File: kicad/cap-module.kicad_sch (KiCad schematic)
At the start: 4 parts, among them U1 RaspberryPi_Pico, U2 AD7747

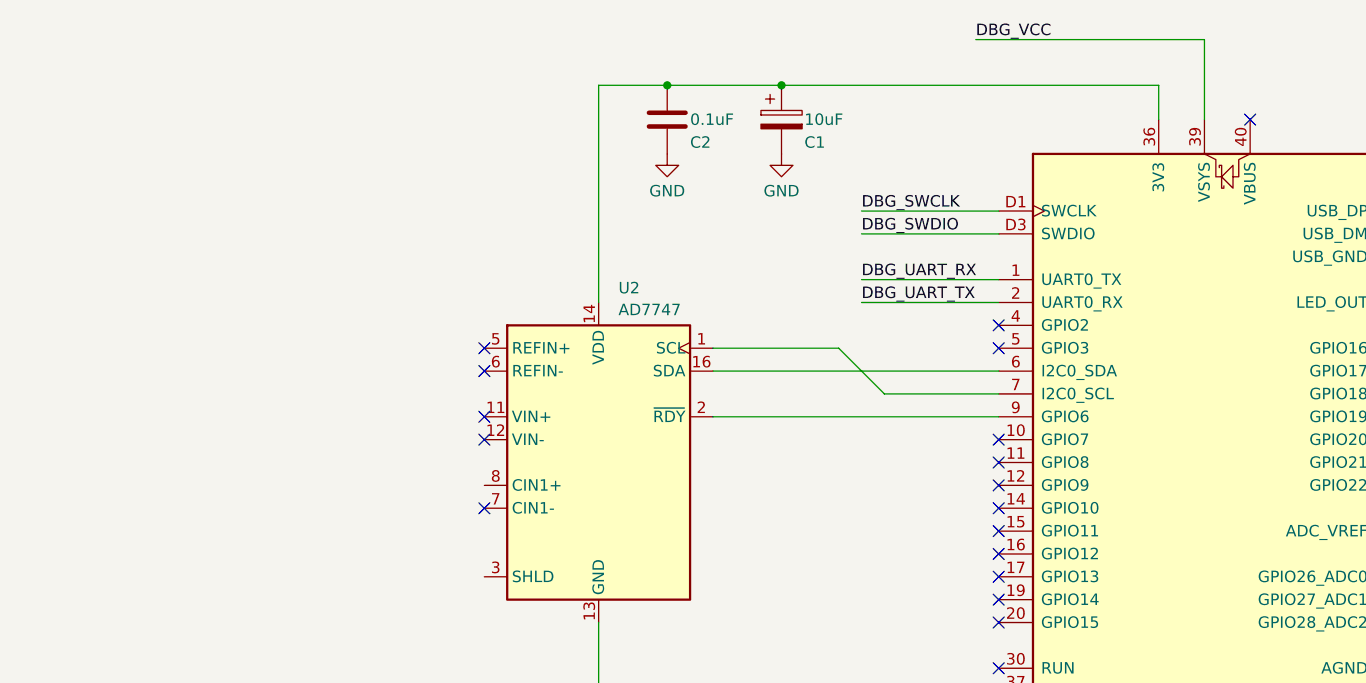
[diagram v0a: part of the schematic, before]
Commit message: Add capacitor socket
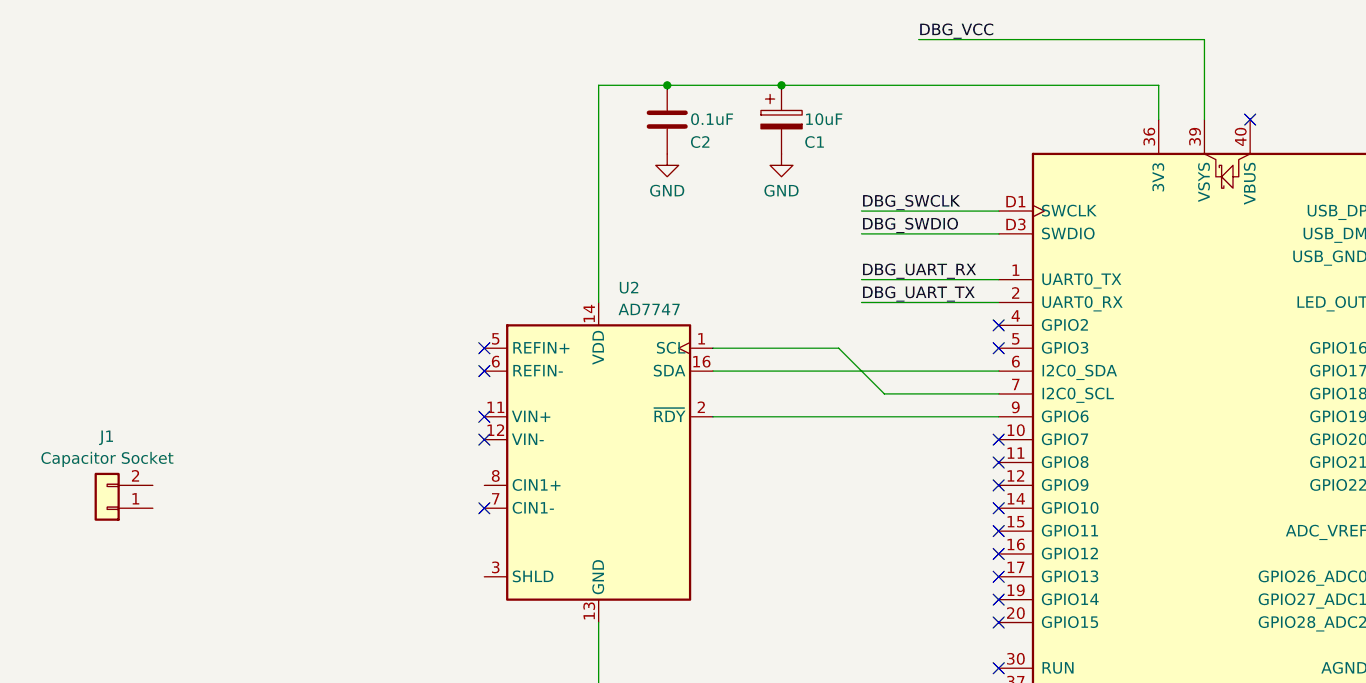
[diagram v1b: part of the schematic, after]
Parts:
- added J1: Capacitor Socket, symbol Connector_Generic:Conn_01x02
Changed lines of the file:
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@@
     (stroke (width 0) (type default))
   )
-  (wire (pts (xy 133.35 50.8) (xy 158.75 50.8))
+  (wire (pts (xy 127 50.8) (xy 158.75 50.8))
     (stroke (width 0) (type default))
   )
@@
     (effects (font (size 1.27 1.27)) (justify left bottom))
   )
-  (label "DBG_VCC" (at 133.35 50.8 0) (fields_autoplaced)
+  (label "DBG_VCC" (at 127 50.8 0) (fields_autoplaced)
     (effects (font (size 1.27 1.27)) (justify left bottom))
   )
@@
         )
       )
+    )
+  )
+  (symbol (lib_id "Connector_Generic:Conn_01x02") (at 36.83 102.87 180) (unit 1)
+    (in_bom yes) (on_board yes) (dnp no) (fields_autoplaced)
+    (property "Reference" "J1" (at 36.83 94.9157 0)
+      (effects (font (size 1.27 1.27)))
+    )
+    (property "Value" "Capacitor Socket" (at 36.83 97.3399 0)
+      (effects (font (size 1.27 1.27)))
+    )
+    (property "Footprint" "" (at 36.83 102.87 0)
+      (effects (font (size 1.27 1.27)) hide)
+    )
+    (property "Datasheet" "~" (at 36.83 102.87 0)
+      (effects (font (size 1.27 1.27)) hide)
+    )
+    (pin "1")
+    (pin "2")
+    (instances
+      (project "cap-module"
+        (path "/2da8fa58-ccef-42b1-8320-baeb3fec91e3"
+          (reference "J1") (unit 1)
+        )
+      )

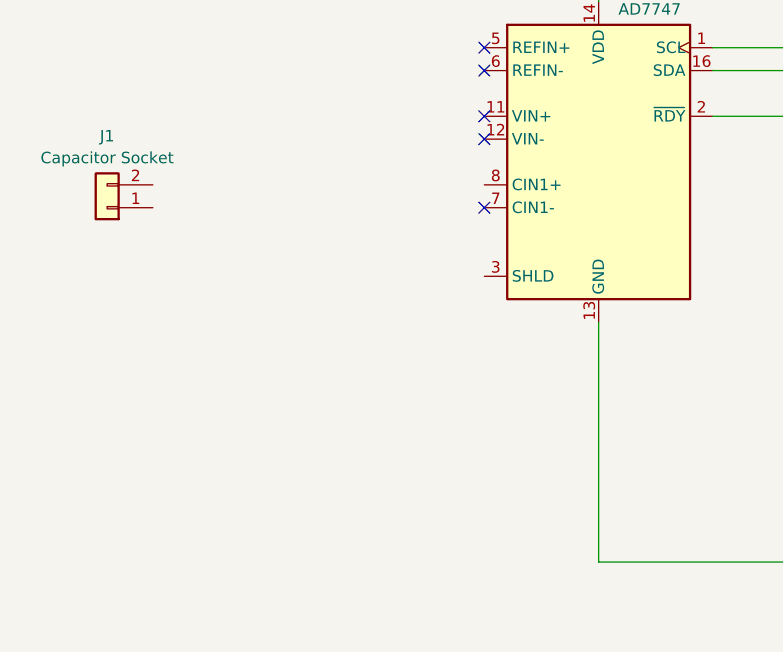
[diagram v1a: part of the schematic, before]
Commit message: Add shielded net & connect capacitor socket
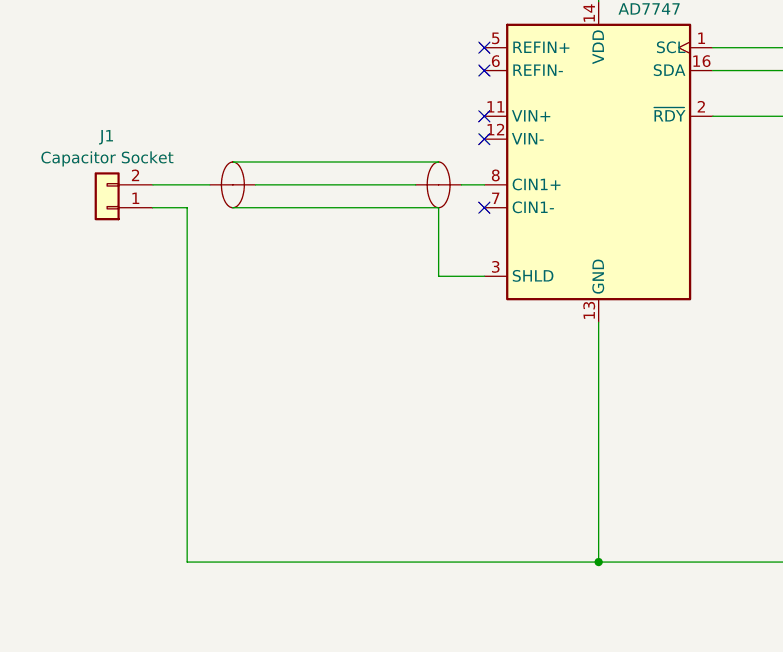
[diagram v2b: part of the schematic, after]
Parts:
- added NS1, NS2: NetShield_1-2SH, symbol Device_NetShield:NetShield_1-2SH
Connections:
- net GND: now also J1.1 (Pin_1)
- net at U2.3 (SHLD): now also NS1.2 (Shield), NS2.2 (Shield)
- net at U2.8 (CIN1+): now also NS1.1
- net at J1.2 (Pin_2): now also NS2.1
- new net: NS1.1, NS2.1
- new net: NS1.2 (Shield), NS2.2 (Shield)
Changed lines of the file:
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@@
   (junction (at 111.76 55.88) (diameter 0) (color 0 0 0 0)
+  )
+  (junction (at 91.44 142.24) (diameter 0) (color 0 0 0 0)
   )
   (junction (at 99.06 55.88) (diameter 0) (color 0 0 0 0)
@@
     (stroke (width 0) (type default))
   )
+  (wire (pts (xy 78.74 100.33) (xy 76.2 100.33))
+    (stroke (width 0) (type default))
+  )
   (wire (pts (xy 91.44 55.88) (xy 99.06 55.88))
     (stroke (width 0) (type default))
   )
+  (wire (pts (xy 45.72 102.87) (xy 45.72 142.24))
+    (stroke (width 0) (type default))
+  )
+  (wire (pts (xy 158.75 50.8) (xy 158.75 59.69))
+    (stroke (width 0) (type default))
+  )
+  (wire (pts (xy 73.66 110.49) (xy 78.74 110.49))
+    (stroke (width 0) (type default))
+  )
+  (wire (pts (xy 153.67 55.88) (xy 153.67 59.69))
+    (stroke (width 0) (type default))
+  )
+  (wire (pts (xy 104.14 85.09) (xy 118.11 85.09))
+    (stroke (width 0) (type default))
+  )
+  (wire (pts (xy 45.72 142.24) (xy 91.44 142.24))
+    (stroke (width 0) (type default))
+  )
+  (wire (pts (xy 41.91 102.87) (xy 45.72 102.87))
+    (stroke (width 0) (type default))
+  )
+  (wire (pts (xy 118.11 85.09) (xy 123.19 90.17))
+    (stroke (width 0) (type default))
+  )
+  (wire (pts (xy 111.76 55.88) (xy 153.67 55.88))
+    (stroke (width 0) (type default))
+  )
+  (wire (pts (xy 127 144.78) (xy 127 142.24))
+    (stroke (width 0) (type default))
+  )
+  (wire (pts (xy 53.34 100.33) (xy 71.12 100.33))
+    (stroke (width 0) (type default))
+  )
+  (wire (pts (xy 158.75 138.43) (xy 158.75 142.24))
+    (stroke (width 0) (type default))
+  )
+  (wire (pts (xy 99.06 55.88) (xy 111.76 55.88))
+    (stroke (width 0) (type default))
+  )
+  (wire (pts (xy 50.8 102.87) (xy 73.66 102.87))
+    (stroke (width 0) (type dash))
+  )
+  (wire (pts (xy 91.44 55.88) (xy 91.44 80.01))
+    (stroke (width 0) (type default))
+  )
+  (wire (pts (xy 120.65 72.39) (xy 135.89 72.39))
+    (stroke (width 0) (type default))
+  )
+  (wire (pts (xy 123.19 90.17) (xy 135.89 90.17))
+    (stroke (width 0) (type default))
+  )
+  (wire (pts (xy 48.26 100.33) (xy 41.91 100.33))
+    (stroke (width 0) (type default))
+  )
+  (wire (pts (xy 120.65 77.47) (xy 135.89 77.47))
+    (stroke (width 0) (type default))
+  )
+  (wire (pts (xy 120.65 80.01) (xy 135.89 80.01))
+    (stroke (width 0) (type default))
+  )
+  (wire (pts (xy 127 142.24) (xy 158.75 142.24))
+    (stroke (width 0) (type default))
+  )
+  (wire (pts (xy 91.44 142.24) (xy 127 142.24))
+    (stroke (width 0) (type default))
+  )
+  (wire (pts (xy 127 50.8) (xy 158.75 50.8))
+    (stroke (width 0) (type default))
+  )
+  (wire (pts (xy 73.66 110.49) (xy 73.66 102.87))
+    (stroke (width 0) (type default))
+  )
+  (wire (pts (xy 50.8 97.79) (xy 73.66 97.79))
+    (stroke (width 0) (type dash))
+  )
   (wire (pts (xy 91.44 115.57) (xy 91.44 142.24))
     (stroke (width 0) (type default))
   )
-  (wire (pts (xy 158.75 50.8) (xy 158.75 59.69))
-    (stroke (width 0) (type default))
-  )
-  (wire (pts (xy 153.67 55.88) (xy 153.67 59.69))
-    (stroke (width 0) (type default))
-  )
-  (wire (pts (xy 104.14 85.09) (xy 118.11 85.09))
-    (stroke (width 0) (type default))
-  )
-  (wire (pts (xy 118.11 85.09) (xy 123.19 90.17))
-    (stroke (width 0) (type default))
-  )
-  (wire (pts (xy 111.76 55.88) (xy 153.67 55.88))
-    (stroke (width 0) (type default))
-  )
-  (wire (pts (xy 127 144.78) (xy 127 142.24))
-    (stroke (width 0) (type default))
-  )
-  (wire (pts (xy 158.75 138.43) (xy 158.75 142.24))
-    (stroke (width 0) (type default))
-  )
-  (wire (pts (xy 99.06 55.88) (xy 111.76 55.88))
-    (stroke (width 0) (type default))
-  )
-  (wire (pts (xy 91.44 55.88) (xy 91.44 80.01))
-    (stroke (width 0) (type default))
-  )
-  (wire (pts (xy 120.65 72.39) (xy 135.89 72.39))
-    (stroke (width 0) (type default))
-  )
-  (wire (pts (xy 123.19 90.17) (xy 135.89 90.17))
-    (stroke (width 0) (type default))
-  )
-  (wire (pts (xy 120.65 77.47) (xy 135.89 77.47))
-    (stroke (width 0) (type default))
-  )
-  (wire (pts (xy 120.65 80.01) (xy 135.89 80.01))
-    (stroke (width 0) (type default))
-  )
-  (wire (pts (xy 127 142.24) (xy 158.75 142.24))
-    (stroke (width 0) (type default))
-  )
-  (wire (pts (xy 91.44 142.24) (xy 127 142.24))
-    (stroke (width 0) (type default))
-  )
-  (wire (pts (xy 127 50.8) (xy 158.75 50.8))
-    (stroke (width 0) (type default))
-  )
   (wire (pts (xy 120.65 69.85) (xy 135.89 69.85))
     (stroke (width 0) (type default))
@@
   (label "DBG_SWDIO" (at 120.65 72.39 0) (fields_autoplaced)
     (effects (font (size 1.27 1.27)) (justify left bottom))
+  )
+  (symbol (lib_id "Device_NetShield:NetShield_1-2SH") (at 73.66 100.33 0) (unit 1)
+    (in_bom no) (on_board yes) (dnp no) (fields_autoplaced)
+    (property "Reference" "NS1" (at 72.39 96.52 0)
+      (effects (font (size 1.27 1.27)) (justify right) hide)
+    )
+    (property "Value" "NetShield_1-2SH" (at 72.39 104.14 0)
+      (effects (font (size 1.27 1.27)) (justify right) hide)
+    )
+    (property "Footprint" "" (at 73.66 100.33 0)
+      (effects (font (size 1.27 1.27)) hide)
+    )
+    (property "Datasheet" "~" (at 73.66 109.22 0)
+      (effects (font (size 1.27 1.27)) hide)
+    )
+    (pin "1")
+    (pin "1")
+    (pin "2")
+    (pin "2")
+    (instances
+      (project "cap-module"
+        (path "/2da8fa58-ccef-42b1-8320-baeb3fec91e3"
+          (reference "NS1") (unit 1)
+        )
+      )
+    )
   )
   (symbol (lib_id "Device:C") (at 99.06 59.69 0) (unit 1)
@@
         )
       )
+    )
+  )
+  (symbol (lib_id "Device_NetShield:NetShield_1-2SH") (at 50.8 100.33 0) (unit 1)
+    (in_bom no) (on_board yes) (dnp no) (fields_autoplaced)
+    (property "Reference" "NS2" (at 49.53 96.52 0)
+      (effects (font (size 1.27 1.27)) (justify right) hide)
+    )
+    (property "Value" "NetShield_1-2SH" (at 49.53 104.14 0)
+      (effects (font (size 1.27 1.27)) (justify right) hide)
+    )
+    (property "Footprint" "" (at 50.8 100.33 0)
+      (effects (font (size 1.27 1.27)) hide)
+    )
+    (property "Datasheet" "~" (at 50.8 109.22 0)
+      (effects (font (size 1.27 1.27)) hide)
+    )
+    (pin "1")
+    (pin "1")
+    (pin "2")
+    (pin "2")
+    (instances
+      (project "cap-module"
+        (path "/2da8fa58-ccef-42b1-8320-baeb3fec91e3"
+          (reference "NS2") (unit 1)
+        )
+      )

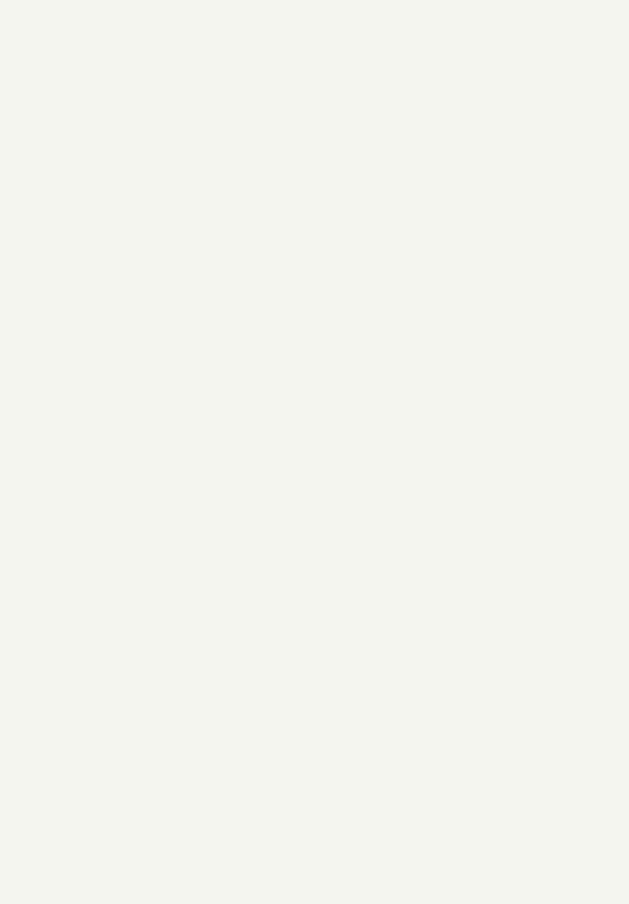
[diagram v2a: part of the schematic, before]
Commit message: Add Picoprobe
Set alternate pin assignments

Note that GND was set to an Input to play nice with the
already-outputting Pico, even though in some cases the Picoprobe
will be supplying power and ground to the system.
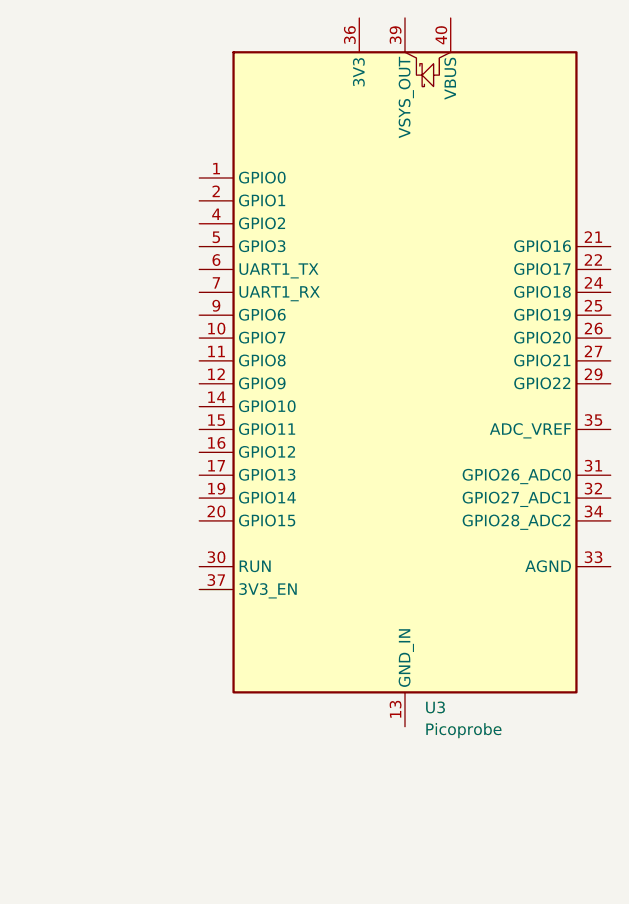
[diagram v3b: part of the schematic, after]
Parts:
- added U3: Picoprobe, Module_RaspberryPi_Pico:RaspberryPi_Pico_Common, symbol MCU_Module_RaspberryPi_Pico:RaspberryPi_Pico
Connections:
- net at NS1.2 (Shield), NS2.2 (Shield): no longer U2.3 (SHLD)
- new net: NS1.2 (Shield), NS2.2 (Shield), U2.3 (SHLD)
- new net: U3.13 (GND), U3.18 (GND), U3.23 (GND), U3.28 (GND), U3.3 (GND), U3.38 (GND), U3.8 (GND)
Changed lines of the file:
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@@
+    )
+  )
+  (symbol (lib_id "MCU_Module_RaspberryPi_Pico:RaspberryPi_Pico") (at 247.65 74.93 0) (unit 1)
+    (in_bom yes) (on_board no) (dnp no) (fields_autoplaced)
+    (property "Reference" "U3" (at 249.8441 110.9401 0)
+      (effects (font (size 1.27 1.27)) (justify left))
+    )
+    (property "Value" "Picoprobe" (at 249.8441 113.3643 0)
+      (effects (font (size 1.27 1.27)) (justify left))
+    )
+    (property "Footprint" "Module_RaspberryPi_Pico:RaspberryPi_Pico_Common" (at 247.65 124.46 0)
+      (effects (font (size 1.27 1.27)) hide)
+    )
+    (property "Datasheet" "https://datasheets.raspberrypi.com/pico/pico-datasheet.pdf" (at 247.65 127 0)
+      (effects (font (size 1.27 1.27)) hide)
+    )
+    (pin "1")
+    (pin "10")
+    (pin "11")
+    (pin "12")
+    (pin "13" (alternate "GND_IN"))
+    (pin "14")
+    (pin "15")
+    (pin "16")
+    (pin "17")
+    (pin "18")
+    (pin "19")
+    (pin "2")
+    (pin "20")
+    (pin "21")
+    (pin "22")
+    (pin "23")
+    (pin "24")
+    (pin "25")
+    (pin "26")
+    (pin "27")
+    (pin "28")
+    (pin "29")
+    (pin "3")
+    (pin "30")
+    (pin "31")
+    (pin "32")
+    (pin "33")
+    (pin "34")
+    (pin "35")
+    (pin "36")
+    (pin "37")
+    (pin "38")
+    (pin "39" (alternate "VSYS_OUT"))
+    (pin "4")
+    (pin "40")
+    (pin "5")
+    (pin "6" (alternate "UART1_TX"))
+    (pin "7" (alternate "UART1_RX"))
+    (pin "8")
+    (pin "9")
+    (instances
+      (project "cap-module"
+        (path "/2da8fa58-ccef-42b1-8320-baeb3fec91e3"
+          (reference "U3") (unit 1)
+        )
+      )
     )
   )

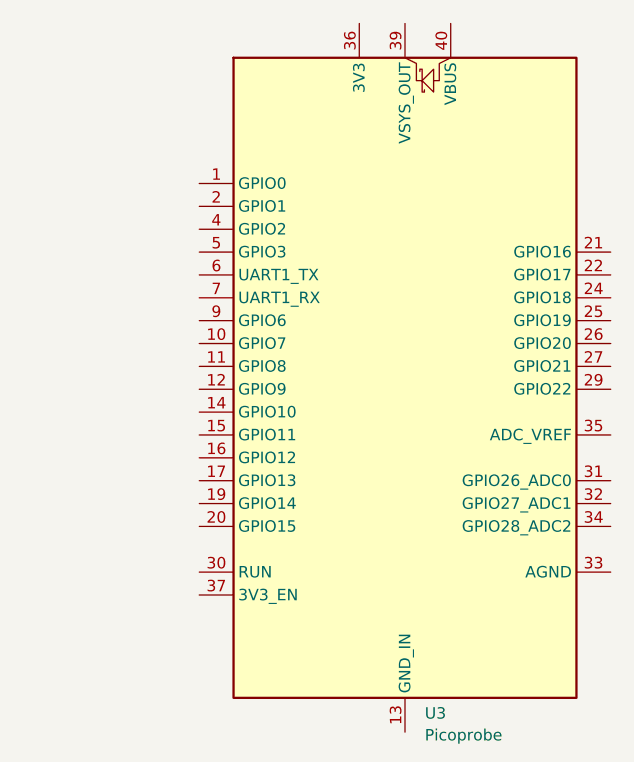
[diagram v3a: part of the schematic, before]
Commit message: Add no-connection flags
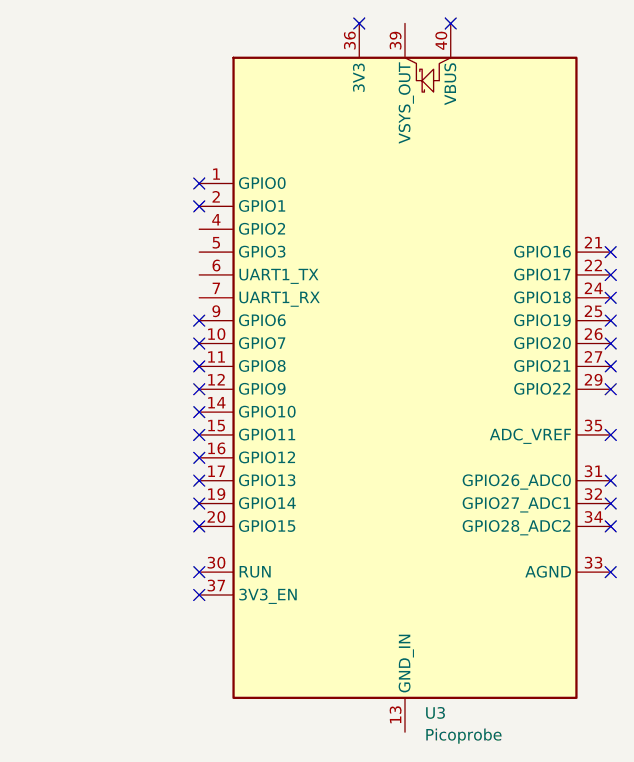
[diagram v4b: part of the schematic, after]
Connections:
- net at NS1.2 (Shield), NS2.2 (Shield): no longer U2.3 (SHLD)
- new net: NS1.2 (Shield), NS2.2 (Shield), U2.3 (SHLD)
- no-connect marks 36 -> 64
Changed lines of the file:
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@@
   (junction (at 127 142.24) (diameter 0) (color 0 0 0 0)
   )
+  (no_connect (at 224.79 52.07))
   (no_connect (at 181.61 92.71))
   (no_connect (at 78.74 102.87))
   (no_connect (at 135.89 123.19))
+  (no_connect (at 224.79 77.47))
+  (no_connect (at 224.79 97.79))
+  (no_connect (at 224.79 69.85))
+  (no_connect (at 224.79 72.39))
   (no_connect (at 135.89 102.87))
+  (no_connect (at 270.51 80.01))
+  (no_connect (at 270.51 87.63))
   (no_connect (at 135.89 100.33))
+  (no_connect (at 270.51 74.93))
   (no_connect (at 181.61 105.41))
+  (no_connect (at 270.51 59.69))
   (no_connect (at 78.74 95.25))
   (no_connect (at 135.89 97.79))
@@
   (no_connect (at 181.61 69.85))
   (no_connect (at 135.89 107.95))
+  (no_connect (at 224.79 80.01))
+  (no_connect (at 224.79 87.63))
+  (no_connect (at 224.79 90.17))
+  (no_connect (at 270.51 64.77))
   (no_connect (at 135.89 128.27))
   (no_connect (at 135.89 95.25))
+  (no_connect (at 252.73 34.29))
   (no_connect (at 135.89 120.65))
   (no_connect (at 181.61 113.03))
+  (no_connect (at 270.51 72.39))
+  (no_connect (at 270.51 67.31))
   (no_connect (at 163.83 59.69))
   (no_connect (at 181.61 95.25))
+  (no_connect (at 270.51 62.23))
+  (no_connect (at 270.51 85.09))
+  (no_connect (at 224.79 95.25))
   (no_connect (at 78.74 85.09))
+  (no_connect (at 224.79 82.55))
   (no_connect (at 181.61 115.57))
   (no_connect (at 135.89 115.57))
+  (no_connect (at 270.51 90.17))
   (no_connect (at 181.61 74.93))
+  (no_connect (at 270.51 69.85))
+  (no_connect (at 242.57 34.29))
   (no_connect (at 78.74 87.63))
   (no_connect (at 135.89 105.41))
   (no_connect (at 181.61 87.63))
+  (no_connect (at 224.79 85.09))
   (no_connect (at 181.61 120.65))
   (no_connect (at 181.61 72.39))
+  (no_connect (at 224.79 67.31))
   (no_connect (at 135.89 82.55))
   (no_connect (at 135.89 113.03))
   (no_connect (at 181.61 110.49))
+  (no_connect (at 270.51 95.25))
   (no_connect (at 181.61 85.09))
+  (no_connect (at 224.79 54.61))
+  (no_connect (at 224.79 74.93))
   (no_connect (at 135.89 85.09))
   (no_connect (at 181.61 97.79))
